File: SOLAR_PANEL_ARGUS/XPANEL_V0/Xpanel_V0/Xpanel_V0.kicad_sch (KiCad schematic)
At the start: 47 parts, among them J1 0530470810, Q1 BSS138, Q2 BSS138, Q4 BSS138, Q5 BSS138, U1 DRV8830DGQ

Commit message: changes made
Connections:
- net torque-coil renamed coils
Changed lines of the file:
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@@
     (effects (font (size 1.016 1.016)) (justify right bottom))
   )
-  (label "torque-coil" (at 107.95 144.018 0) (fields_autoplaced)
+  (label "coils" (at 107.95 144.018 0) (fields_autoplaced)
     (effects (font (size 1.27 1.27)) (justify left bottom))
   )

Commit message: made changes
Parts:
- removed BT1, BT2, BT3, BT4, BT5: SM141K06L, SM141K06L:SOLAR_SM141K06L, symbol SM141K06L:SM141K06L
- removed D? (x6): SBD, Diode_SMD:D_PowerDI-123, symbol Device:D_Schottky
- removed J1: 0530470810, 0530470810:MOLEX_0530470810, symbol Connector8_0530470810:0530470810
- added B1, B10, B11, B12, B2, B3, B4, B5, B6, B7, B8, B9: KXOB25-05X3F-TR, CHIP2_KXOB25-05X3F-TR_AAR, symbol KXOB25-05X3TF-TR:KXOB25-05X3F-TR
- added D1: BAT120C_115, BAT120C_115:SOT230P700X180-4N, symbol BAT120C:BAT120C_115
- added J2: F3311A7H121014E200, F3311A7H121014E200, symbol F3311A7H121008E200:F3311A7H121014E200
- added JP1, JP2: ~, SparkFun-Jumper:SMT-JUMPER_3_NO_NO-SILK, symbol SparkFun-Jumper:SolderJumper_3_Open_No_Silk
- added Q7, Q8, Q9: KXOB201K04F-TR, TRAN_KXOB201K04F-TR_AAR, symbol KXOB201K04TF-TR:KXOB201K04F-TR
- added U2: OPT4001DTST, DTS0008A-MFG, symbol OPT4001DTST:OPT4001DTST
- added U3: LTC3130EUDC-1-PBF, UDC_20_ADI, symbol LTC3130:LTC3130EUDC-1-PBF
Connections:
- net GND: now also B7.2, J2.13, J2.14, J2.MP1, J2.MP2, JP2.1 (A), Q7.2, U2.4 (GND)
- net SCL: now also JP1.3 (B), U2.5 (SCL)
- net SCL1_b4iso: now also J2.3
- net SDA: now also JP1.1 (A), U2.8 (SDA)
- net SDA1_b4iso: now also J2.4
- net VBATT: now also J2.7
- net VSOLAR: now also D1.4, J2.1, J2.2
- new net: B3.2, B8.1
- new net: B8.2, B9.1
- new net: B11.2, B5.1
- new net: B5.2, B6.1
- new net: Q7.1, Q8.2
- new net: JP1.2 (C), JP2.2 (C), U2.2 (ADDR)
- new net: B10.2, B4.1
- new net: B12.1, B4.2
- new net: B1.2, B2.1
- new net: D1.1, Q9.1
- new net: B2.2, B3.1
- new net: B11.1, B12.2
- new net: B10.1, B9.2
- new net: B6.2, B7.1
- new net: Q8.1, Q9.2
- new net +3.3v: JP2.3 (B), U2.1 (VDD)
- new net ARR1: B1.1, D1.3
- no-connect marks 1 -> 2
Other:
- note added: "SUN SENSOR"
- moved on the sheet: C2, C?, D7, D8, L?, Q1, Q2, Q4, Q5, Q?A, Q?B, R?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

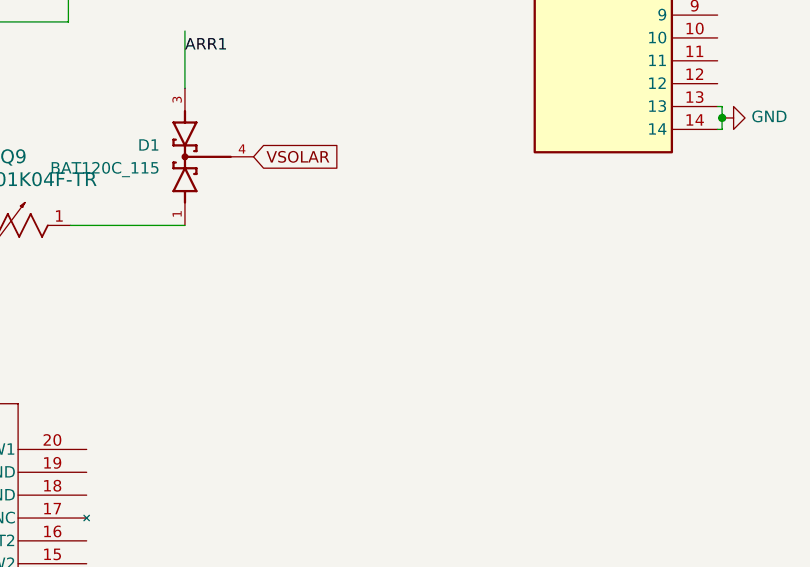
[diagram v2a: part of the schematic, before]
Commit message: made custom footprints and symbols for both solar panels-custom lib also created and added to files
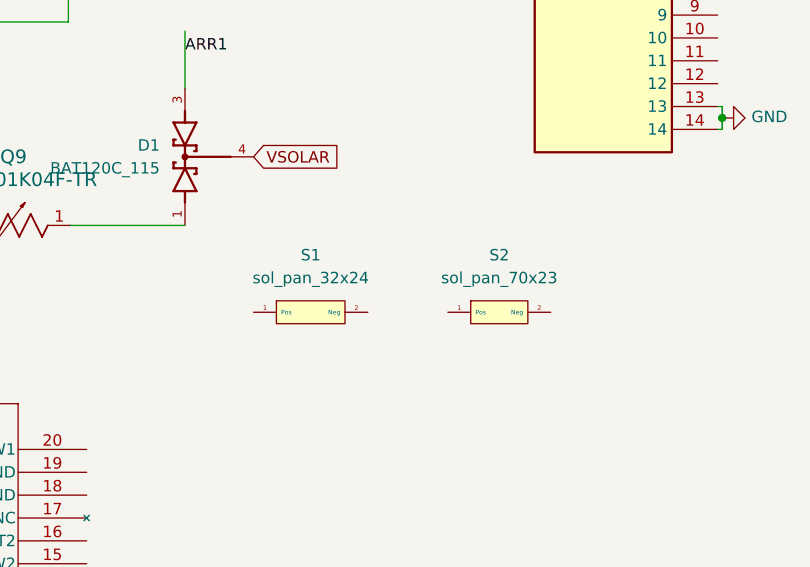
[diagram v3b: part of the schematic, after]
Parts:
- added S1: sol_pan_32x24, custom_solar_panel_footprint:solar_panel_SM500K12TF_32x24, symbol solar_symbol_lib:sol_pan_32x24
- added S2: sol_pan_70x23, custom_solar_panel_footprint:sol_pan_SM141K10TFS_70x23, symbol solar_symbol_lib:sol_pan_70x23
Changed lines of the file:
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@@
+    )
+  )
+  (symbol (lib_id "solar_symbol_lib:sol_pan_32x24") (at 129.54 80.01 0) (unit 1)
+    (in_bom yes) (on_board yes) (dnp no) (fields_autoplaced)
+    (property "Reference" "S1" (at 130.81 77.47 0)
+      (effects (font (size 1.27 1.27)))
+    )
+    (property "Value" "sol_pan_32x24" (at 130.81 80.01 0)
+      (effects (font (size 1.27 1.27)))
+    )
+    (property "Footprint" "custom_solar_panel_footprint:solar_panel_SM500K12TF_32x24" (at 134.62 88.9 0)
+      (effects (font (size 1.27 1.27)) hide)
+    )
+    (property "Datasheet" "" (at 129.54 80.01 0)
+      (effects (font (size 1.27 1.27)) hide)
+    )
+    (pin "1")
+    (pin "2")
+    (instances
+      (project "Xpanel_V0"
+        (path "/97119169-578f-44be-8822-faf8f0e4fcd6"
+          (reference "S1") (unit 1)
+        )
+      )
     )
   )
@@
         )
       )
+    )
+  )
+  (symbol (lib_id "solar_symbol_lib:sol_pan_70x23") (at 151.13 83.82 0) (unit 1)
+    (in_bom yes) (on_board yes) (dnp no) (fields_autoplaced)
+    (property "Reference" "S2" (at 151.765 77.47 0)
+      (effects (font (size 1.27 1.27)))
+    )
+    (property "Value" "sol_pan_70x23" (at 151.765 80.01 0)
+      (effects (font (size 1.27 1.27)))
+    )
+    (property "Footprint" "custom_solar_panel_footprint:sol_pan_SM141K10TFS_70x23" (at 151.13 88.9 0)
+      (effects (font (size 1.27 1.27)) hide)
+    )
+    (property "Datasheet" "" (at 151.13 83.82 0)
+      (effects (font (size 1.27 1.27)) hide)
+    )
+    (pin "1")
+    (pin "2")
+    (instances
+      (project "Xpanel_V0"
+        (path "/97119169-578f-44be-8822-faf8f0e4fcd6"
+          (reference "S2") (unit 1)
+        )
+      )
